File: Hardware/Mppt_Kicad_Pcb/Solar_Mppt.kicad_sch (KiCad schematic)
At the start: 18 parts, among them Q1 SL102N10, Q1.a1 SL102N10, Q2 SL102N10, Q2.a1 SL102N10, Q3 SL102N10, Q3.a1 SL102N10, Q4 SL102N10, Q4.a1 SL102N10

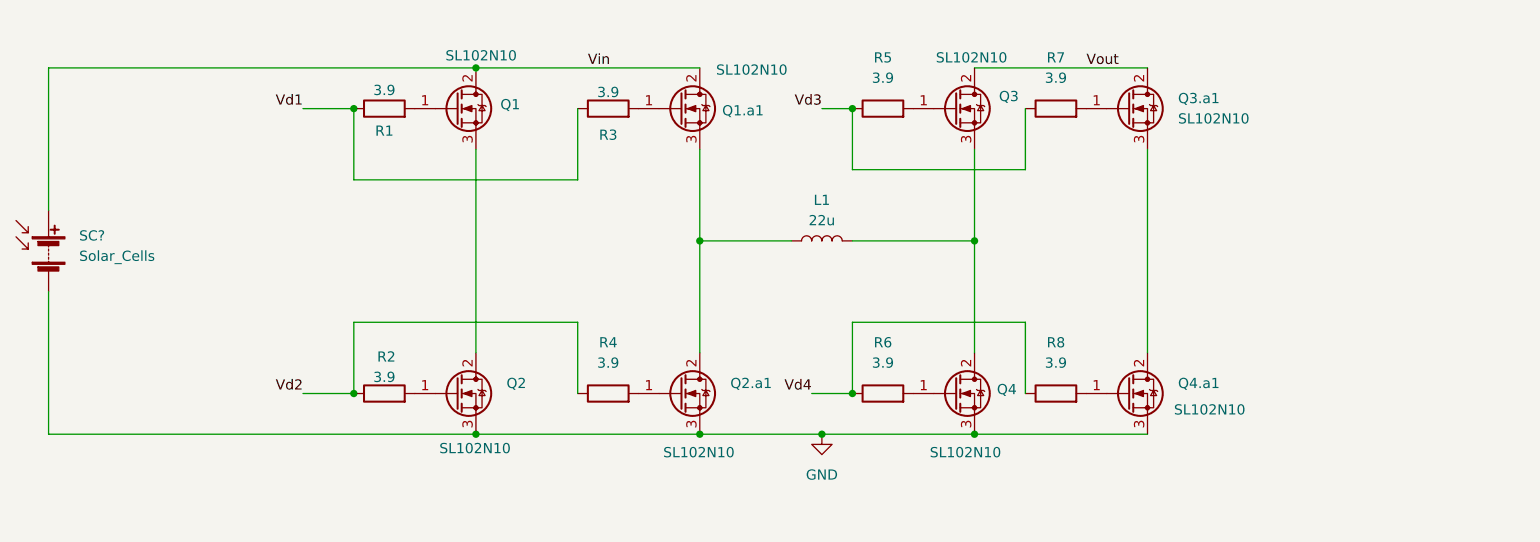
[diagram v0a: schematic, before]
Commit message: updated schematics
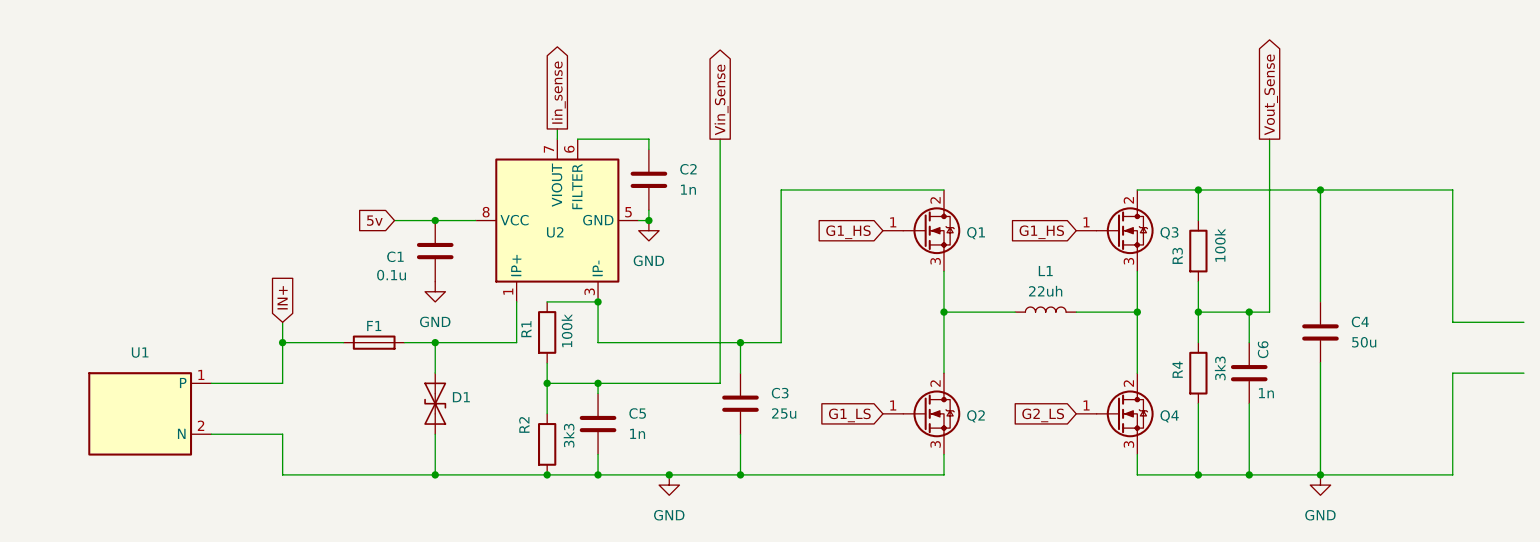
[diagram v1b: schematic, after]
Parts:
- removed Q1.a1, Q2.a1, Q3.a1, Q4.a1: SL102N10, symbol Transistor_FET:IRF740
- removed R5, R6, R7, R8: 3.9, symbol Device:R
- removed SC?: Solar_Cells, symbol Device:Solar_Cells
- added C1: 0.1u, symbol Device:C
- added C2, C5, C6: 1n, symbol Device:C
- added C3: 25u, symbol Device:C
- added C4: 50u, symbol Device:C
- added D1: ESD9B5.0ST5G, Diode_SMD:D_SOD-923, symbol Diode:ESD9B5.0ST5G
- added F1: Fuse, symbol Device:Fuse
- added U1: (no value), symbol Mppt_symbols:Connector
- added U2: ACS712xLCTR-20A, Package_SO:SOIC-8_3.9x4.9mm_P1.27mm, symbol Sensor_Current:ACS712xLCTR-20A
- L1: value 22u -> 22uh
- R1, R3: value 3.9 -> 100k
- R2, R4: value 3.9 -> 3k3
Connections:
- net Vin is gone; now on an unnamed net: Q1.2 (D)
- net GND: now also R2.2, R4.2, C1.2, C2.2, C3.2, C4.2, C5.2, C6.2, D1.2 (A2), U1.2 (N), U2.5 (GND)
- net G2_LS: now reaches Q4.1 (G)
- net G1_HS: now reaches Q3.1 (G)
- net G1_HS: now also Q1.1 (G)
- net Vout_Sense: now reaches R3.2
- net Vout_Sense: now also R4.1, C6.1
- net at L1.1: now also Q1.3 (S), Q2.2 (D)
- net Vin_Sense: now reaches R1.2
- net Vin_Sense: now also R2.1, C5.1; no longer Q1.1 (G)
- net G1_LS: now reaches Q2.1 (G)
- net G1_LS: no longer R2.2
- net Vd1: no longer names the net of R1.1
- net Vd1: now also C3.1, U2.3 (IP-), U2.4 (IP-); no longer R3.1
- removed net Vd2: R2.1, R4.1
- net Vout: no longer names the net of Q3.2 (D)
- net Vout: now also R3.1, C4.1
- new net: D1.1 (A1), F1.2, U2.1 (IP+), U2.2 (IP+)
- new net: C2.1, U2.6 (FILTER)
- new net 5v: C1.1, U2.8 (VCC)
- new net IN+: F1.1, U1.1 (P)
- new net Iin_sense: U2.7 (VIOUT)
